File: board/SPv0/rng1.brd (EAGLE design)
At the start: 52 x 50.5 mm, 29 parts, among them IC1 TL084D

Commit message: reducing to original circuit
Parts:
- removed C4: 4.7u, rcl:C0805
- removed JP1: (no value), pinhead:1X03
- removed R13: 100K, rcl:R0805
- removed TP1: PTR1PAD1-13, testpad:P1-13
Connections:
- removed net AOUT_1: JP1.1, T5.B
- removed net AOUT_2: IC1.12, JP1.3, R13.2
- removed net DOUT_2: IC1.14, TP1.TP
- removed net N$13: C4.1, IC1.13, R13.1
- net AOUT: now also T5.B; no longer JP1.2
- net GND: no longer C4.2
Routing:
- net GND: track 123.3 -> 0.00 mm, vias 2 -> 0
- net VCC: track 89.6 -> 0.00 mm, vias 2 -> 0
- net VREF: track 60.3 -> 0.00 mm
- net N$12: track 56.0 -> 0.00 mm
- net N$4: track 41.9 -> 0.00 mm, vias 2 -> 0
- net AOUT_2: track 41.4 -> 0.00 mm
- net N$2: track 34.2 -> 0.00 mm, vias 2 -> 0
- net AOUT_1: track 31.9 -> 0.00 mm, vias 2 -> 0
- net AOUT: track 31.8 -> 0.00 mm
- net N$13: track 15.7 -> 0.00 mm
- net N$7: track 14.4 -> 0.00 mm
- net N$9: track 13.1 -> 0.00 mm
- net N$14: track 11.7 -> 0.00 mm
- net N$8: track 10.8 -> 0.00 mm
- net N$1: track 9.78 -> 0.00 mm
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
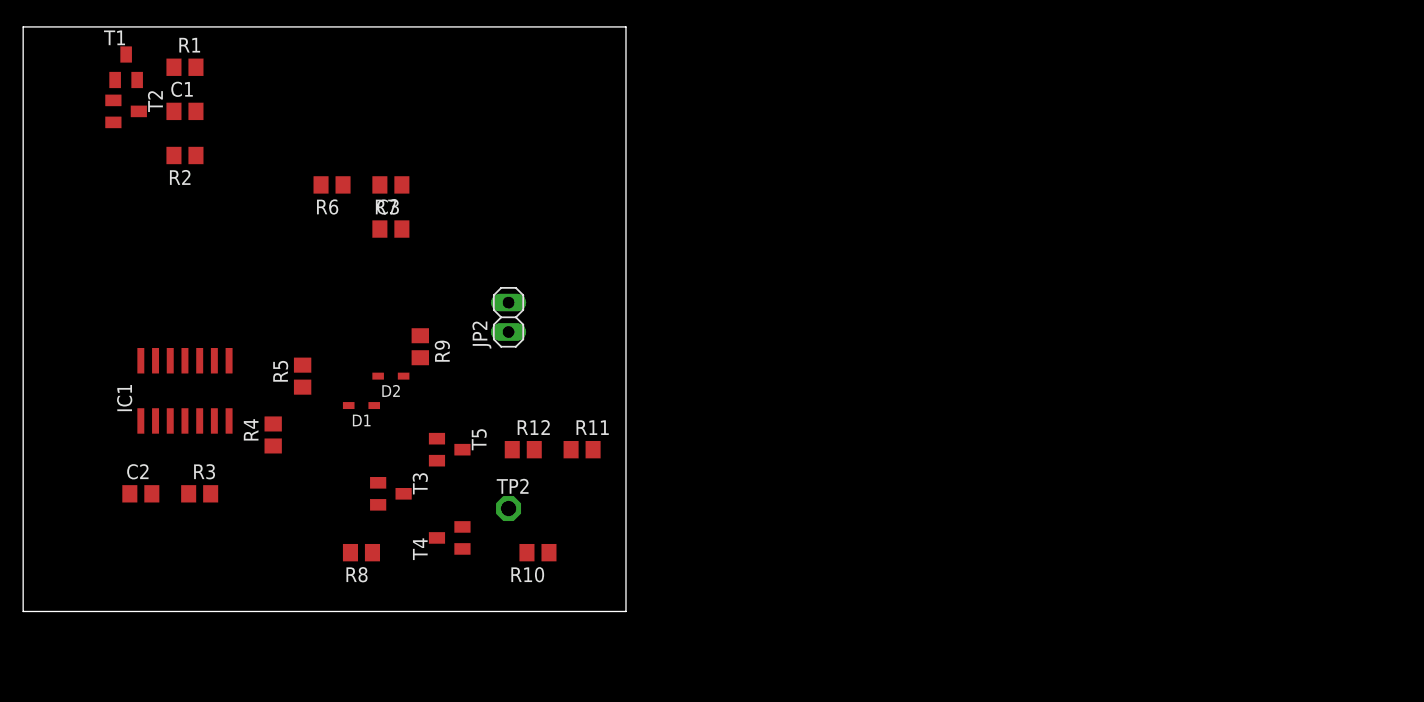
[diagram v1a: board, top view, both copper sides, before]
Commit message: going with the avalanche noise for v0 starting in on initial layout of board
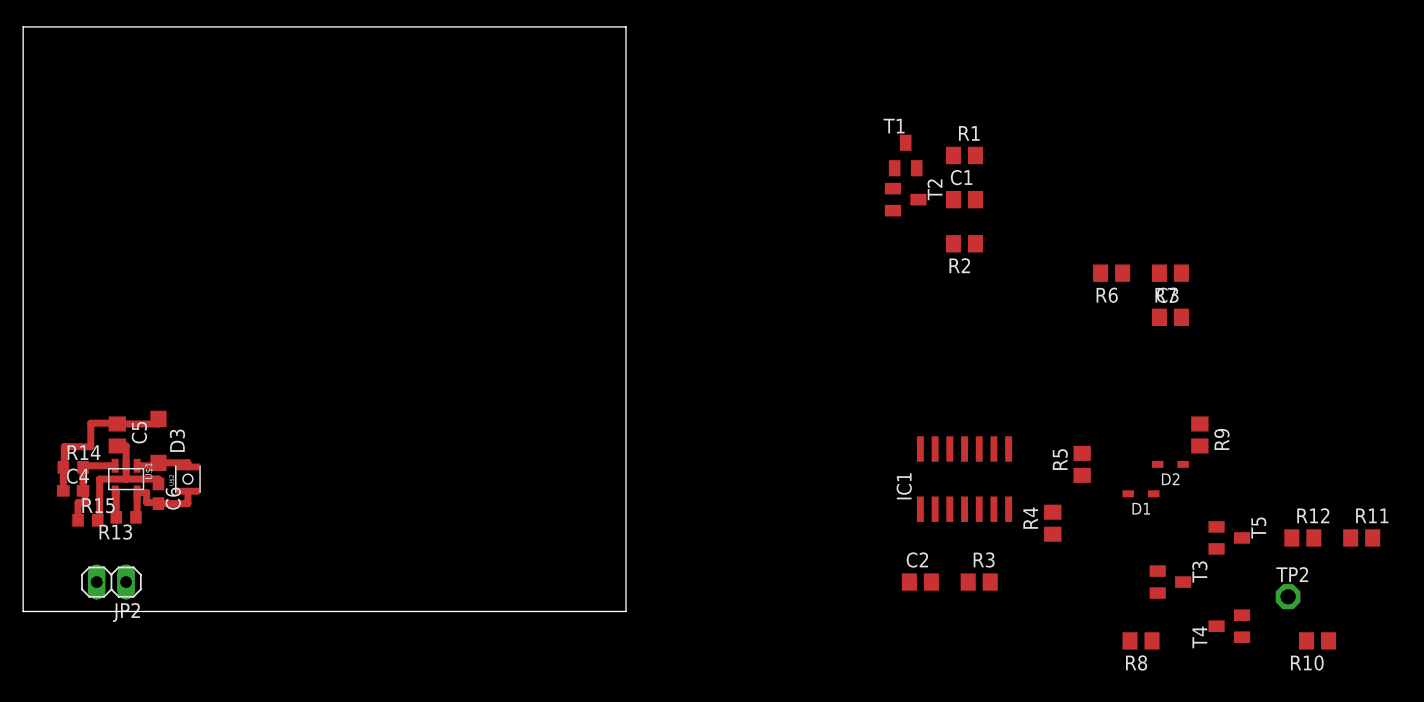
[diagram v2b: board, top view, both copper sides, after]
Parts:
- added C4: 120pF, rcl:C0603
- added C5: 4.7uF, rcl:C0805
- added C6: 2.2uF, rcl:C0603
- added D3: (no value), diode:SOD123
- added R13: 51K, rcl:R0603
- added R14: 205K, rcl:R0603
- added R15: 13.3K, rcl:R0603
- added U$1: LM27313, rng:SOT-23-5
- added U$2: 10uH, rng:L1007
- IC1: value TL084D -> LM339D
- T1, T2: value (none) -> n3904
- T3, T4, T5: value (none) -> n3906
- moved C3 67.7 mm to (99.1, 25.4)
- moved R1 67.7 mm to (81.3, 39.4)
- moved T1 67.7 mm to (76.2, 39.4)
- moved C1 67.7 mm to (81.3, 35.6)
- moved C2 67.7 mm to (77.5, 2.54)
- moved D1 67.7 mm to (96.5, 10.2)
- moved D2 67.7 mm to (99.1, 12.7)
- moved IC1 67.7 mm to (81.3, 11.4)
- moved R10 67.7 mm to (111.8, -2.54)
- moved R11 67.7 mm to (115.6, 6.35)
- moved R12 67.7 mm to (110.5, 6.35)
- moved R2 67.7 mm to (81.3, 31.8)
- moved R3 67.7 mm to (82.5, 2.54)
- moved R4 67.7 mm to (88.9, 7.62)
- moved R5 67.7 mm to (91.4, 12.7)
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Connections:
- new net N$13: R13.2, U$1.P$4
- new net N$17: D3.A, U$1.P$1, U$2.P$2
- new net N$18: C4.2, R14.2, R15.1, U$1.P$3
- new net VDD: C4.1, C5.1, D1.2, D3.C, IC1.3, R1.2, R14.1, R6.2, R8.2
- net AOUT: now also IC1.1; no longer IC1.7
- net GND: now also C5.2, C6.1, IC1.12, R15.2, U$1.P$2; no longer IC1.11
- net N$2: now also IC1.9; no longer IC1.10
- net N$4: now also IC1.5; no longer IC1.3
- net N$5: now also IC1.4; no longer IC1.1
- net N$8: now also IC1.7; no longer IC1.5
- net VCC: now also C6.2, R13.1, U$1.P$5, U$2.P$1; no longer D1.2, IC1.4, R1.2, R6.2, R8.2
- net VREF: now also IC1.14; no longer IC1.9
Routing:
- net VDD: track 0.00 -> 14.6 mm
- net GND: track 0.00 -> 12.8 mm
- net VCC: track 0.00 -> 8.68 mm
- net N$18: track 0.00 -> 8.24 mm
- net N$17: track 0.00 -> 4.99 mm
- net N$13: track 0.00 -> 2.25 mm

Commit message: fxing up library parts added prototype for read parameter page
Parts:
- removed D1, D2: (no value), zetex:SOD323
- removed R10, R9: 10K, rcl:R0805
- removed R11, R12: 5K, rcl:R0805
- removed R8: 1.2K, rcl:R0805
- removed T3, T4, T5: n3906, transistor:SOT23-BEC
- removed TP2: PTR1PAD1-13, testpad:P1-13
- added TP1, TP3, TP5: TPSQPAD1-13, testpad:P1-13
- C4, C6: device rcl:C0603 -> Passives:R0805
- C5: device rcl:C0805 -> Passives:R0805
- IC1: value LM339D -> TL084D
- R1, R2, R3, R4, R5, R6, R7: device rcl:R0805 -> Passives:R0805
- R13, R14, R15: device rcl:R0603 -> Passives:R0805
- moved C3 83.1 mm to (16.5, 15.5), turned to 270 degrees
- moved R7 82.0 mm to (18.5, 13.7), turned to 270 degrees
- moved R6 76.3 mm to (18.5, 17.5), turned to 270 degrees
- moved R4 60.4 mm to (30.0, 20.8), turned to 270 degrees
- moved R5 60.0 mm to (32.0, 20.6), turned to 270 degrees
- moved R2 58.0 mm to (24.1, 21.6), turned to 270 degrees
- moved IC1 57.2 mm to (24.1, 14.7), turned to 90 degrees
- moved R1 52.9 mm to (38.4, 8.38), turned to 90 degrees
- moved T1 50.7 mm to (34.0, 11.2)
- moved T2 50.7 mm to (34.3, 7.11)
- moved C2 48.2 mm to (29.7, 9.40), turned to 90 degrees
- moved C1 47.3 mm to (40.9, 10.9), turned to 90 degrees
- moved R3 45.3 mm to (39.1, 15.5), turned to 270 degrees
- moved JP2 3.06 mm to (7.87, 5.59)
- moved C5 0.80 mm to (8.89, 15.5), turned to 90 degrees
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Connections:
- removed net DOUT_1: R11.1, R12.2, TP2.TP
- removed net N$10: D1.1, D2.2
- removed net N$11: R8.1, T3.E
- removed net N$12: T3.C, T4.E, T5.E
- removed net N$14: R10.2, T4.C
- removed net N$15: R12.1, T5.C
- removed net N$9: D2.1, R9.2, T3.B
- net AOUT: now also IC1.7, R4.P$2, TP1.TP; no longer IC1.1, R4.2, T5.B
- net GND: now also C5.P$2, C6.P$1, IC1.11, IC1.13, R15.P$2, R7.P$1; no longer C5.2, C6.1, R10.1, R11.2, R15.2, R7.1, R9.1
- net N$1: now also R1.P$1; no longer R1.1
- net N$13: now also R13.P$2; no longer R13.2
- net N$18: now also C4.P$2, R14.P$2, R15.P$1; no longer C4.2, R14.2, R15.1
- net N$2: now also IC1.10, R6.P$1, R7.P$2; no longer IC1.9, R6.1, R7.2
- net N$4: now also IC1.3, R2.P$1; no longer IC1.5, R2.1
- net N$5: now also IC1.1, TP3.TP; no longer IC1.4
- net N$6: now also R3.P$1; no longer R3.1
- net N$7: now also R3.P$2, R4.P$1; no longer R3.2, R4.1
- net N$8: now also IC1.5, R5.P$1; no longer IC1.7, R5.1
- net VCC: now also C6.P$2, R13.P$1; no longer C6.2, R13.1
- net VDD: now also C4.P$1, C5.P$1, IC1.4, R1.P$2, R14.P$1, R6.P$2, TP5.TP; no longer C4.1, C5.1, D1.2, IC1.3, R1.2, R14.1, R6.2, R8.2
- net VREF: now also IC1.9, R2.P$2, R5.P$2; no longer IC1.14, R2.2, R5.2, T4.B
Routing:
- net VDD: track 14.6 -> 60.1 mm, vias 0 -> 4
- net GND: track 12.8 -> 46.9 mm
- net N$4: track 0.00 -> 29.8 mm
- net VREF: track 0.00 -> 16.9 mm
- net N$7: track 0.00 -> 15.4 mm
- net N$6: track 0.00 -> 10.9 mm
- net N$1: track 0.00 -> 9.00 mm
- net N$2: track 0.00 -> 7.10 mm
- net N$8: track 0.00 -> 6.85 mm
- net N$5: track 0.00 -> 6.38 mm
- net AOUT: track 0.00 -> 5.51 mm
- net N$3: track 0.00 -> 2.02 mm
- net VCC: track 8.68 -> 10.5 mm
- net N$18: track 8.24 -> 7.13 mm
